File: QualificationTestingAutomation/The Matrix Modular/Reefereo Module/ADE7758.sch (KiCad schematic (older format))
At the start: 28 parts, among them J10 Conn_01x01_Female, J4 Conn_01x01_Female, J5 Conn_01x01_Female, J7 Conn_01x01_Female, J8 Conn_01x01_Female, J9 Conn_01x01_Female, T1 CST2010_Split, T2 CST2010_Split, T3 CST2010_Split, U10 ADE7758

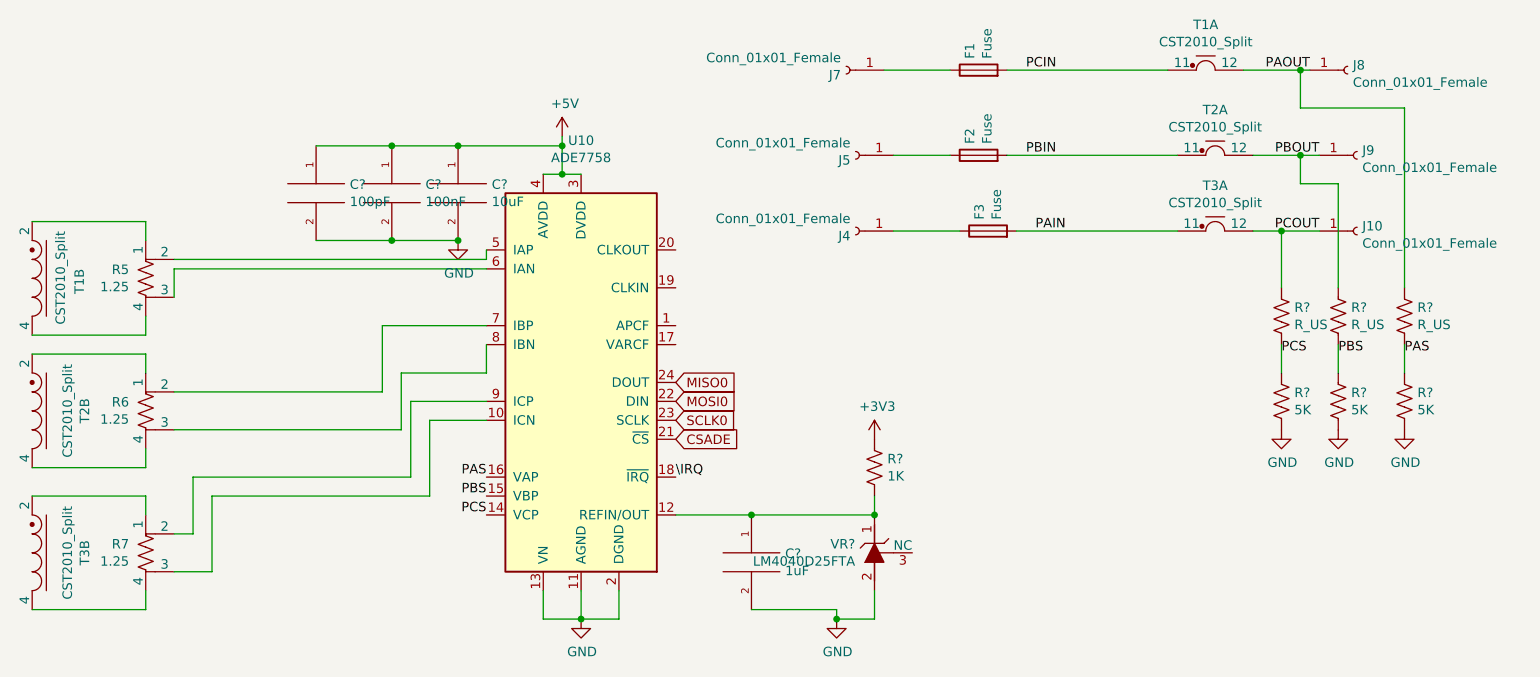
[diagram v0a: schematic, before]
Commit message: Reefero Module PCB design
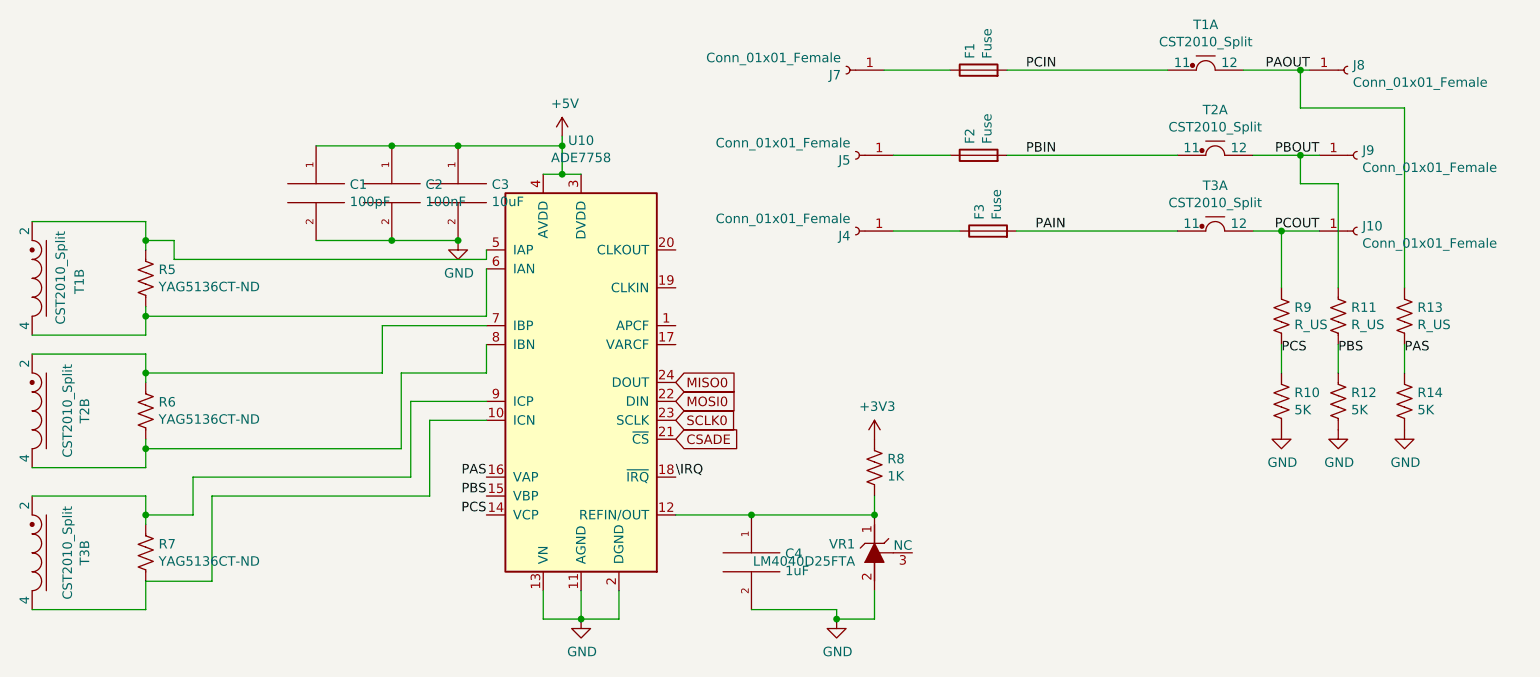
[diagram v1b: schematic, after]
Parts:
- removed R5, R6, R7: 1.25, symbol Device:R_Shunt_US
- added R5, R6, R7: YAG5136CT-ND, Resistor_SMD:R_2512_6332Metric_Pad1.52x3.35mm_HandSolder, symbol Device:R_US
- C1, C2: renamed from C?; footprint (none) -> .pretty:C_0402_1005Metric
- C3, C4: renamed from C?; footprint (none) -> .pretty:0805
- F1, F2, F3: footprint (none) -> Fuse:0606LittleFuse
- J10, J4, J5, J7, J8, J9: footprint (none) -> Connector_Wire:SolderWirePad_1x01_SMD_5x10mm
- R10, R11, R12, R13, R14, R9: renamed from R?; footprint (none) -> Resistor_SMD:R_2512_6332Metric_Pad1.52x3.35mm_HandSolder
- R8: renamed from R?; footprint (none) -> .pretty:C_0402_1005Metric
- gave numbers to parts that had none: 1
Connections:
- net at U10.10 (ICN): now also T3.4, R7.2
- net at U10.5 (IAP): now also T1.2, R5.1
- net at U10.6 (IAN): now also T1.4, R5.2
- net at U10.7 (IBP): now also T2.2, R6.1
- net at U10.8 (IBN): now also T2.4, R6.2
- net at U10.9 (ICP): now also T3.2, R7.1
